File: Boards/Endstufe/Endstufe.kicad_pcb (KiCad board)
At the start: 2 copper layers, 74 parts, among them P1 CONN_3, P3 Relais, P4 6V3_AC, P5 Trafo_GK, P6 6V3_DC, P7 CONN_4, Q1 2SC2979, Q2 MJE5731, T1 KT88, T2 KT88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

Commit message: Anoden-Stabi auf eigenes Board, Endstufe Layouttest
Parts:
- removed C14, C19: 10µF/400V, Capacitors_Elko_ThroughHole:Elko_vert_25x12.5mm_RM5
- removed C15, C17, C20: 47µF/400V, Capacitors_Elko_ThroughHole:Elko_vert_31.5x16mm_RM7.5
- removed C16, C18, C21: 1µF/400V, Capacitors_ThroughHole:C_Rect_L32_W15_P27
- removed D1, D2: BZT03-C150, Diodes_ThroughHole:Diode_DO-41_SOD81_Horizontal_RM10
- removed D3: BZT03-C120, Diodes_ThroughHole:Diode_DO-41_SOD81_Horizontal_RM10
- removed LOGO1: OPEN_HARDWARE_1, Symbols:Symbol_OSHW-Logo_CopperTop
- removed Q1: 2SC2979, w_to:to220-horiz_5772
- removed Q2: MJE5731, w_to:to220-horiz_5772
- removed R24: 82k, Resistors_ThroughHole:Resistor_Horizontal_RM10mm
- removed R25: 10k/1W, Resistors_ThroughHole:Resistor_Horizontal_RM15mm
- removed R26, R28, R30: 1k5, Resistors_ThroughHole:Resistor_Horizontal_RM10mm
- removed R27: 33k, Resistors_ThroughHole:Resistor_Horizontal_RM10mm
- removed R29, R31: 30k, Resistors_ThroughHole:Resistor_Horizontal_RM10mm
- added P2: Trafo, Sockets_WAGO734:WAGO_734_5pin_Straight, F.Cu at (200.9, 97.8)
- added P8: Vsup2, Sockets_Mini-Universal:MiniUniversalMate-N-LokSocket_2PinVertical, F.Cu at (147.8, 107.4)
- added P9: VSup3, Sockets_Mini-Universal:MiniUniversalMate-N-LokSocket_4PinVertical, F.Cu at (145.5, 94.2)
- C11, C2, C4, C8: footprint Capacitors_ThroughHole:C_Rect_L18_W5_P15 -> w_capacitors:CPA_8x21MM
- C7: footprint Capacitors_ThroughHole:C_Disc_D6_P5 -> w_capacitors:CPA_8x21MM
- P4, P5, P6: footprint MiniUniversalMate-N-LokSockets_13Aug2012:MiniUniversalMate-N-LokSocket_2PinVertical_12Aug2012 -> Sockets_Mini-Universal:MiniUniversalMate-N-LokSocket_2PinVertical
- P7: value CONN_4 -> VSup1; footprint MiniUniversalMate-N-LokSockets_13Aug2012:MiniUniversalMate-N-LokSocket_4PinVertical_13Aug2012 -> Sockets_Mini-Universal:MiniUniversalMate-N-LokSocket_2PinVertical
- moved R23 296.8 mm to (215.4, 130.6)
- moved C12 292.6 mm to (204.7, 120.9)
- moved RV5 268.6 mm to (206.8, 114.3), turned to 270 degrees
- moved R13 259.0 mm to (178.8, 153.4)
- moved R10 250.7 mm to (178.8, 86.4)
- moved C13 250.2 mm to (160.0, 136.7), turned to 270 degrees
- moved C9 243.0 mm to (147.3, 137.7)
- moved R20 242.4 mm to (169.2, 113.8), turned to 180 degrees
- moved R15 240.9 mm to (219.5, 111.8)
- moved RV4 233.7 mm to (147.3, 121.9), turned to 180 degrees
- moved R5 233.5 mm to (162.1, 53.3)
- moved C1 214.1 mm to (158.5, 69.6), turned to 270 degrees
- moved C5 197.2 mm to (140.2, 76.7), turned to 180 degrees
- moved R4 188.9 mm to (137.2, 117.9), turned to 90 degrees
- moved RV1 185.9 mm to (139.7, 61.0), turned to 180 degrees
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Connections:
- R10 pad 2: (no net) -> Net-(P2-Pad2)
- R13 pad 2: (no net) -> Net-(P2-Pad4)
- T1 pad 3: (no net) -> Net-(P2-Pad1)
- T2 pad 3: (no net) -> Net-(P2-Pad5)
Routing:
- net 6V3: track 0.00 -> 149.8 mm
- net Net-(P4-Pad1): track 0.00 -> 100.4 mm, vias 0 -> 2
- net Net-(C1-Pad2): track 0.00 -> 90.2 mm
- net Net-(C11-Pad1): track 0.00 -> 80.1 mm
- net Net-(C3-Pad1): track 0.00 -> 67.3 mm
- net Net-(C10-Pad1): track 0.00 -> 66.2 mm
- net Net-(P2-Pad4): track 0.00 -> 59.9 mm
- net Net-(P4-Pad2): track 0.00 -> 50.4 mm
- net Net-(P2-Pad5): track 0.00 -> 48.9 mm
- net Net-(C3-Pad2): track 0.00 -> 46.9 mm
- net Net-(C2-Pad2): track 0.00 -> 45.4 mm
- net Net-(C7-Pad2): track 0.00 -> 37.9 mm
- net Net-(C12-Pad2): track 0.00 -> 35.9 mm
- net Net-(C13-Pad1): track 0.00 -> 34.2 mm
- net Net-(C1-Pad1): track 0.00 -> 32.4 mm
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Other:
- net class Default: via_dia 0.6 -> 1; via_drill 0.4 -> 0.8
- net class HV added: clearance 0.8, trace_width 0.5, via_dia 1, via_drill 0.8
- net class Heizung added: clearance 0.5, trace_width 1.2, via_dia 1, via_drill 0.8
- net class Signal added: clearance 0.5, trace_width 1, via_dia 1, via_drill 0.8

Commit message: Layouting...
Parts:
- removed P8: Vsup2, Sockets_Mini-Universal:MiniUniversalMate-N-LokSocket_2PinVertical
- added R24: 1M, Resistors_ThroughHole:Resistor_Horizontal_RM10mm, F.Cu at (130.3, 66.0)
- moved C7 135.6 mm to (59.6, 156.2)
- moved P1 135.6 mm to (62.6, 178.6)
- moved P3 135.6 mm to (43.3, 179.1)
- moved R9 135.6 mm to (74.3, 169.9)
- moved RL1 135.6 mm to (56.5, 165.9)
- moved P9 62.6 mm to (93.5, 128.9), turned to 270 degrees
- moved C12 37.4 mm to (241.6, 127.3)
- moved P5 37.4 mm to (256.3, 127.3)
- moved R23 37.4 mm to (252.2, 136.9)
- moved R15 36.0 mm to (255.3, 115.8)
- moved RV5 35.8 mm to (242.3, 118.1)
- moved P7 30.3 mm to (194.1, 107.2), turned to 270 degrees
- moved RV3 22.9 mm to (181.9, 82.3)
- moved R11 22.1 mm to (54.1, 109.2), turned to 270 degrees
- moved R13 21.2 mm to (198.8, 146.3), turned to 90 degrees
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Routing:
- net 6V3: track 149.8 -> 0.00 mm
- net Net-(C3-Pad1): track 67.3 -> 0.00 mm
- net Net-(C10-Pad1): track 66.2 -> 0.00 mm
- net Net-(P4-Pad2): track 50.4 -> 102.9 mm
- net Net-(C3-Pad2): track 46.9 -> 0.00 mm
- net Net-(C2-Pad2): track 45.4 -> 0.00 mm
- net Net-(C11-Pad1): track 80.1 -> 37.4 mm
- net Net-(C7-Pad2): track 37.9 -> 0.00 mm
- net Net-(C12-Pad2): track 35.9 -> 0.00 mm
- net Net-(C1-Pad2): track 90.2 -> 54.4 mm
- net Net-(C7-Pad1): track 32.3 -> 0.00 mm
- net Net-(C10-Pad2): track 31.3 -> 0.00 mm
- net Net-(P2-Pad1): track 21.1 -> 50.8 mm
- net Net-(R12-Pad1): track 29.3 -> 0.00 mm
- net Net-(P2-Pad4): track 59.9 -> 31.2 mm
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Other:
- net class Default: clearance 0.2 -> 0.5; trace_width 0.25 -> 0.5
- rule trace_clearance: 0.2 -> 0.5

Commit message: Updated Layout
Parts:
- moved R23 133.3 mm to (120.7, 158.4)
- moved R15 133.1 mm to (125.1, 143.8), turned to 180 degrees
- moved RV5 128.9 mm to (117.5, 150.1)
- moved P5 121.2 mm to (137.2, 149.5), turned to 270 degrees
- moved P1 118.0 mm to (87.0, 63.1), turned to 0 degrees
- moved C12 113.5 mm to (130.2, 148.8), turned to 270 degrees
- moved P3 111.0 mm to (48.3, 68.2), turned to 270 degrees
- moved C7 84.9 mm to (57.1, 71.4), turned to 270 degrees
- moved R9 78.7 mm to (65.4, 91.7), turned to 0 degrees
- moved RL1 77.4 mm to (46.4, 89.2), turned to 270 degrees
- moved R6 11.2 mm to (65.4, 86.0), turned to 0 degrees
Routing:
- net -120V: track 0.00 -> 189.3 mm
- net Net-(C12-Pad1): track 0.00 -> 108.3 mm, vias 0 -> 2
- net Net-(P6-Pad2): track 0.00 -> 107.6 mm
- net 6V3: track 0.00 -> 89.7 mm
- net Net-(C3-Pad1): track 0.00 -> 77.1 mm
- net +300V: track 0.00 -> 54.7 mm
- net -60V: track 16.5 -> 69.5 mm
- net Net-(C10-Pad1): track 0.00 -> 47.8 mm
- net Net-(C7-Pad2): track 0.00 -> 45.3 mm
- net Net-(R11-Pad1): track 0.00 -> 44.7 mm
- net Net-(C11-Pad1): track 37.4 -> 72.6 mm
- net Net-(C2-Pad2): track 0.00 -> 33.6 mm
- net Net-(C10-Pad2): track 0.00 -> 32.1 mm
- net +240V: track 0.00 -> 32.0 mm
- net Net-(C12-Pad2): track 0.00 -> 29.5 mm
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
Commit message: Work in Progress
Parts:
- moved R8 51.5 mm to (154.4, 94.0), turned to 180 degrees
- moved RV1 43.2 mm to (154.4, 86.4)
- moved R7 28.4 mm to (149.4, 79.2)
- moved P4 20.9 mm to (173.2, 111.3)
- moved R2 20.4 mm to (149.4, 74.7)
- moved RV3 18.6 mm to (173.7, 99.1)
- moved R10 15.4 mm to (185.6, 86.9)
- moved R5 15.2 mm to (140.2, 54.4), turned to 0 degrees
- moved T1 11.9 mm to (177.8, 66.3)
- moved C5 11.3 mm to (149.4, 68.1)
- moved C1 10.5 mm to (149.4, 62.5)
- moved R14 7.74 mm to (151.9, 121.9), turned to 0 degrees
- moved R24 2.79 mm to (130.3, 63.2)
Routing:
- net Net-(C7-Pad2): track 45.3 -> 111.8 mm, vias 0 -> 2
- net Net-(C3-Pad2): track 23.6 -> 48.3 mm, vias 0 -> 2
- net Net-(P6-Pad2): track 107.6 -> 127.6 mm, vias 0 -> 2
- net Net-(P4-Pad1): track 100.8 -> 82.6 mm
- net Net-(C1-Pad1): track 54.3 -> 37.2 mm
- net Net-(P2-Pad2): track 36.9 -> 21.7 mm
- net -60V: track 69.5 -> 84.1 mm
- net Net-(P2-Pad1): track 50.8 -> 38.2 mm
- net Net-(C3-Pad1): track 77.1 -> 66.6 mm
- net Net-(P4-Pad2): track 103.1 -> 92.8 mm
- net Net-(C5-Pad1): track 24.3 -> 16.8 mm
- net Net-(R14-Pad2): track 4.63 -> 9.21 mm
- net Net-(R10-Pad1): track 7.26 -> 11.3 mm
- net Net-(R11-Pad1): track 44.7 -> 48.3 mm
- net Net-(R8-Pad1): track 3.61 -> 6.25 mm
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- added copper zone on B.Cu, net GND

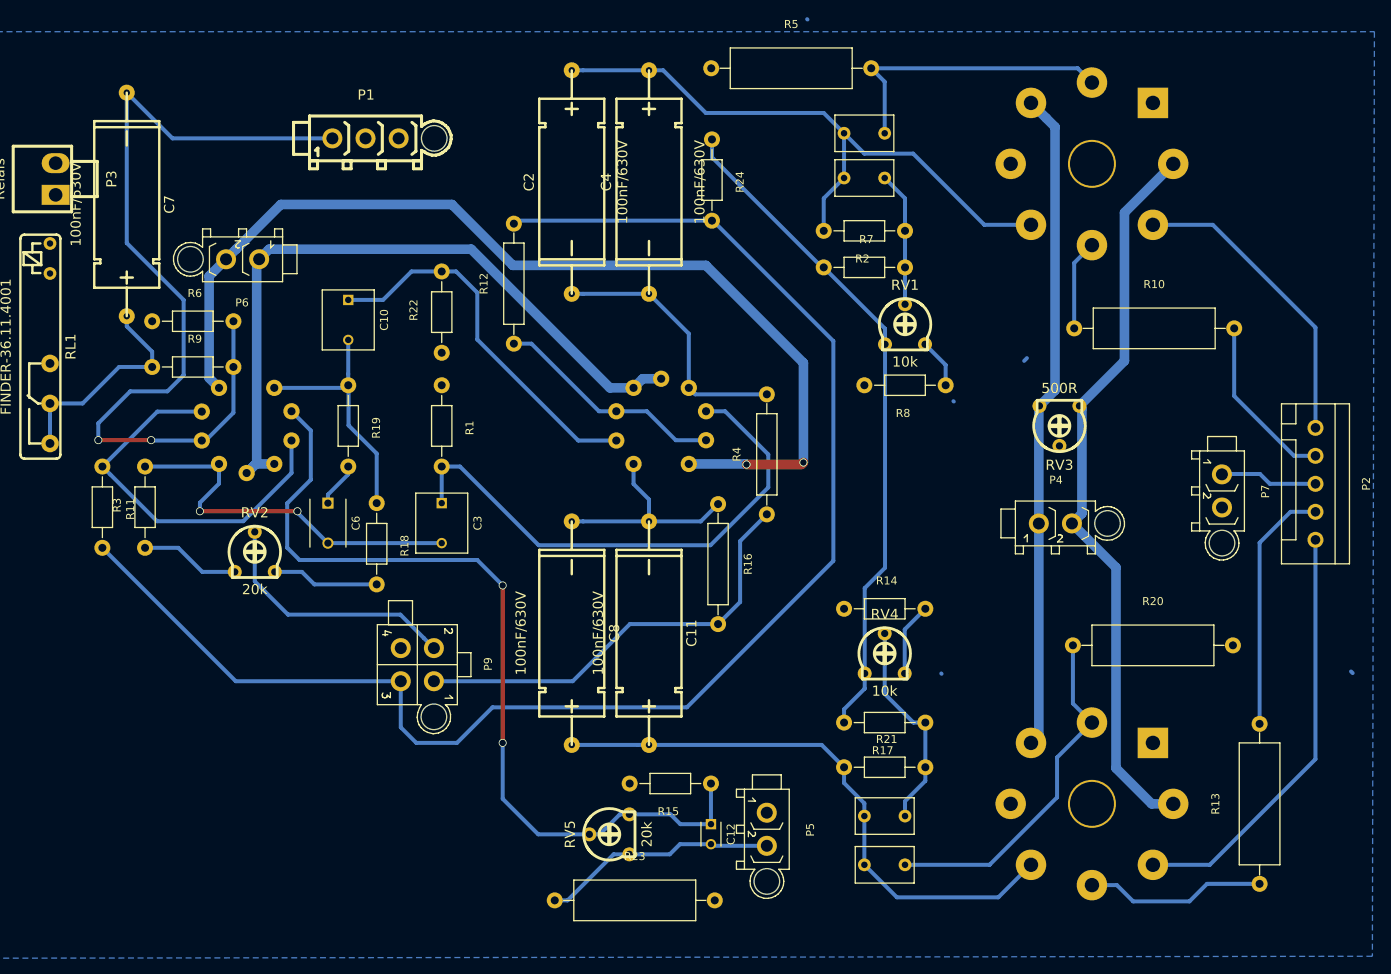
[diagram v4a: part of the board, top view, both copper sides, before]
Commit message: Bias-Anzeige erstellt
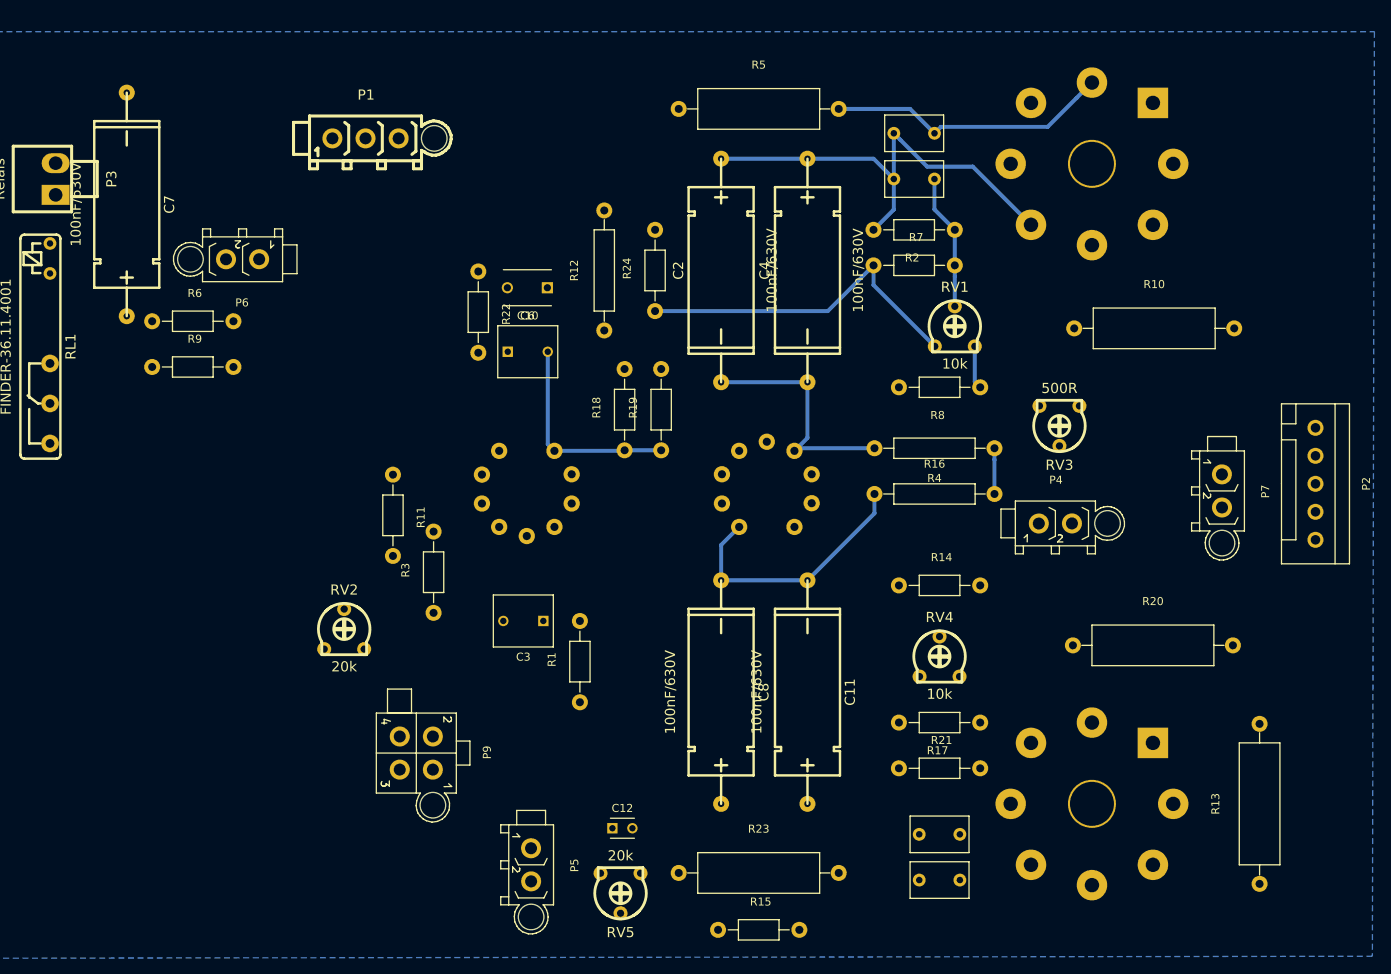
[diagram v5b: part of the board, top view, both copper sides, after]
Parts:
- moved R19 39.2 mm to (124.0, 97.0), turned to 90 degrees
- moved C6 38.4 mm to (109.7, 81.8), turned to 180 degrees
- moved R3 37.0 mm to (95.5, 117.3)
- moved R11 36.3 mm to (90.4, 110.2)
- moved U2 35.9 mm to (107.2, 106.9)
- moved R18 35.2 mm to (119.4, 97.0), turned to 90 degrees
- moved R1 34.2 mm to (113.8, 128.5), turned to 90 degrees
- moved P5 29.8 mm to (107.7, 153.9)
- moved R16 28.4 mm to (158.1, 107.6), turned to 0 degrees
- moved C4 22.7 mm to (142.2, 79.6)
- moved R24 22.6 mm to (123.2, 84.7), turned to 90 degrees
- moved C2 21.7 mm to (131.4, 79.6)
- moved R15 21.4 mm to (136.1, 162.1), turned to 0 degrees
- moved C11 21.1 mm to (142.2, 132.3)
- moved R4 21.0 mm to (158.1, 101.9), turned to 180 degrees
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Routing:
- net -120V: track 188.1 -> 0.00 mm
- net Net-(P6-Pad2): track 127.6 -> 0.00 mm, vias 2 -> 0
- net Net-(C7-Pad2): track 111.8 -> 0.00 mm, vias 2 -> 0
- net Net-(C12-Pad1): track 109.3 -> 0.00 mm, vias 2 -> 0
- net Net-(P4-Pad2): track 92.8 -> 0.00 mm
- net 6V3: track 89.7 -> 0.00 mm
- net Net-(P4-Pad1): track 82.6 -> 0.00 mm
- net Net-(C11-Pad1): track 72.6 -> 0.00 mm
- net Net-(C3-Pad1): track 66.6 -> 0.00 mm
- net Net-(P2-Pad5): track 53.2 -> 0.00 mm
- net +300V: track 54.7 -> 5.72 mm
- net Net-(R11-Pad1): track 48.3 -> 0.00 mm
- net Net-(C3-Pad2): track 48.3 -> 0.00 mm, vias 2 -> 0
- net Net-(C10-Pad1): track 47.2 -> 0.00 mm
- net Net-(C13-Pad1): track 44.3 -> 0.00 mm
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
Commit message: Work in Progress
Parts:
- removed RL1: FINDER-36.11.4001, w_relay:relay_34.51
- removed RV1, RV4: 10k, w_pth_resistors:trimmer_piher_pt6xv
- added C14: 10µF / 100V, Capacitors_ThroughHole:C_Radial_D6.3_L11.2_P2.5, F.Cu at (158.0, 101.6)
- added C15: 10µF / 100V, Capacitors_ThroughHole:C_Radial_D6.3_L11.2_P2.5, F.Cu at (158.0, 117.9)
- added K1: DIP 7212-D, Reed:REED, F.Cu at (72.6, 128.5)
- added P8: Bias, Pin_Headers:Pin_Header_Straight_2x03_Pitch2.54mm, F.Cu at (149.9, 101.1)
- C1, C13, C5, C9: value 68pF -> 68pF / 500V; footprint Capacitor-Wima-FKP2-630v:Capacitor-Wima-FKP2-630v-R5B4K5 -> Capacitors_ThroughHole:C_Disc_D7.5_P5
- C10, C3: value 100nF -> 100nF / 400V; footprint Capacitors_ThroughHole:C_Rect_L7.5_W6.5_P5 -> Capacitors_ThroughHole:C_Axial_D8_L21_P28
- C11, C2, C4, C8: value 100nF/630V -> 100nF/400V; footprint w_capacitors:CPA_8x21MM -> Capacitors_ThroughHole:C_Axial_D8_L21_P28
- C12: value 100pF -> 100pF / 500V; footprint Capacitors_ThroughHole:C_Disc_D3_P2.5 -> Capacitors_ThroughHole:C_Disc_D7.5_P5
- C6: value 33pF -> 33pF / 500V
- C7: value 100nF/630V -> 100nF; footprint w_capacitors:CPA_8x21MM -> Capacitors_ThroughHole:C_Disc_D3_P2.5
- R10, R13, R20, R23, R5: footprint Resistors_ThroughHole:Resistor_Horizontal_RM20mm -> Resistors_ThroughHole:Resistor_Ceramic_Horizontal_L23mm-W9mm-H9mm-p30mm
- R24: value 1M -> 30k
- R9: value 68k -> 220R
- RV2, RV3, RV5: footprint w_pth_resistors:trimmer_piher_pt6xv -> w_pth_resistors:trimmer_piher_pt10xv10
- moved P9 75.0 mm to (66.0, 70.1), turned to 180 degrees
- moved R4 70.5 mm to (96.5, 67.6), turned to 90 degrees
- moved P3 61.3 mm to (59.1, 128.5)
- moved R16 60.9 mm to (106.7, 140.2), turned to 180 degrees
- moved P6 57.0 mm to (115.6, 114.6), turned to 0 degrees
- moved P1 54.3 mm to (55.9, 107.6), turned to 90 degrees
- moved R15 50.2 mm to (94.0, 134.9), turned to 90 degrees
- moved R19 49.0 mm to (74.9, 97.4), turned to 270 degrees
- moved R18 46.4 mm to (74.9, 83.8)
- moved RV2 45.0 mm to (65.0, 83.8), turned to 270 degrees
- moved RV5 42.9 mm to (86.4, 129.5), turned to 180 degrees
- moved C6 39.9 mm to (82.3, 110.8), turned to 270 degrees
- moved R23 37.3 mm to (99.1, 151.4)
- moved P5 35.3 mm to (72.6, 149.4)
- moved R3 32.2 mm to (70.1, 97.5), turned to 270 degrees
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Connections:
- net Net-(C1-Pad1) renamed Bias_1
- net Net-(C13-Pad1) renamed Bias_2
- C5 pad 1: Net-(C5-Pad1) -> UG_1
- C9 pad 2: Net-(C9-Pad2) -> UG_2
- P1 pad 1: Net-(C7-Pad2) -> Net-(P1-Pad1)
- P9 pad 3: -120V -> GND
- P9 pad 4: GND -> -120V
- R14 pad 1: GND -> UG_2
- R17 pad 1: Net-(C9-Pad2) -> UG_2
- R2 pad 1: Net-(C5-Pad1) -> UG_1
- R21 pad 2: Net-(C9-Pad2) -> UG_2
- R7 pad 2: Net-(C5-Pad1) -> UG_1
- R8 pad 1: Net-(R8-Pad1) -> UG_1
- R8 pad 2: GND -> Net-(C14-Pad1)
- R9 pad 1: Net-(C7-Pad1) -> Net-(P1-Pad1)
- R9 pad 2: Net-(C7-Pad2) -> Net-(C7-Pad1)
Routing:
- net -120V: track 0.00 -> 126.4 mm, vias 0 -> 2
- net +300V: track 5.72 -> 113.8 mm
- net Net-(P4-Pad2): track 0.00 -> 90.2 mm
- net Net-(P6-Pad2): track 0.00 -> 87.7 mm, vias 0 -> 4
- net Net-(P4-Pad1): track 0.00 -> 85.1 mm
- net 6V3: track 0.00 -> 82.3 mm, vias 0 -> 4
- net Bias_2: track 0.00 -> 75.4 mm
- net Bias_1: track 35.5 -> 108.4 mm, vias 0 -> 2
- net Net-(C12-Pad1): track 0.00 -> 70.0 mm
- net Net-(P2-Pad5): track 0.00 -> 51.5 mm
- net Net-(C3-Pad2): track 0.00 -> 51.3 mm
- net Net-(C2-Pad2): track 30.2 -> 80.3 mm
- net Net-(C11-Pad1): track 0.00 -> 44.4 mm
- net Net-(P2-Pad1): track 0.00 -> 38.8 mm
- net Net-(C7-Pad2): track 0.00 -> 34.3 mm
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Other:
- board outline added: 163.6 x 110.2 mm

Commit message: Work in Progress
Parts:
- removed P1: CONN_3, MiniUniversalMate-N-LokSockets_13Aug2012:MiniUniversalMate-N-LokSocket_3PinVertical_12Aug2012
- removed P3: Relais, w_conn_kk156:kk156_26-60-4020
- removed P9: VSup3, Sockets_Mini-Universal:MiniUniversalMate-N-LokSocket_4PinVertical
- added J1: HV In, Connectors_Mini-Universal:MiniUniversalMate-N-LokSocket_6PinVertical, F.Cu at (78.1, 67.6)
- added J2: Relais, Connectors_Molex:Molex_KK-6410-02_02x2.54mm_Straight, F.Cu at (58.4, 127.0)
- added J3: NF_In, Connectors_Molex:Molex_KK-6410-02_02x2.54mm_Straight, F.Cu at (58.4, 112.8)
- added REF**: MountingHole_3.2mm_M3_DIN965, Mounting_Holes:MountingHole_3.2mm_M3_DIN965, F.Cu at (202.8, 157.0)
- added REF**: MountingHole_3.2mm_M3_DIN965, Mounting_Holes:MountingHole_3.2mm_M3_DIN965, F.Cu at (202.8, 57.0)
- added REF**: MountingHole_3.2mm_M3_DIN965, Mounting_Holes:MountingHole_3.2mm_M3_DIN965, F.Cu at (58.8, 57.0)
- added REF**: MountingHole_3.2mm_M3_DIN965, Mounting_Holes:MountingHole_3.2mm_M3_DIN965, F.Cu at (58.8, 157.1)
- K1: value DIP 7212-D -> G6E; footprint Reed:REED -> Relays_THT:Relay_SPDT_OMRON-G6E
- moved K1 7.22 mm to (69.2, 122.2)
- moved R13 4.83 mm to (200.9, 135.6)
- moved RV2 2.59 mm to (67.6, 83.3), turned to 180 degrees
- moved R18 0.51 mm to (74.9, 83.3)
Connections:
- net 6V3 renamed Net-(P6-Pad1)
- K1 pad 1: Net-(C7-Pad1) -> Net-(J2-Pad1)
- K1 pad 6: (no net) -> Net-(J2-Pad2)
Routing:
- net -120V: track 126.4 -> 110.2 mm
- net Net-(J2-Pad2): track 0.00 -> 13.0 mm
- net Net-(J2-Pad1): track 0.00 -> 12.8 mm
- net Net-(R18-Pad2): track 5.97 -> 12.1 mm
- net Net-(R13-Pad1): track 31.5 -> 26.7 mm
- net +300V: track 113.8 -> 109.7 mm
- net Net-(C7-Pad1): track 27.7 -> 30.9 mm
- net Net-(J3-Pad1): track 10.7 -> 7.69 mm
- net Net-(P2-Pad4): track 14.7 -> 17.5 mm
- net Net-(R3-Pad1): track 6.28 -> 8.35 mm
- net Net-(P2-Pad5): track 51.5 -> 53.5 mm
- net Net-(C3-Pad1): track 32.8 -> 34.6 mm
- net Net-(C2-Pad2): track 80.3 -> 81.8 mm
- net Net-(C12-Pad1): track 70.0 -> 71.0 mm
- net +240V: track 15.1 -> 16.0 mm
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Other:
- board text added: "Bot"
